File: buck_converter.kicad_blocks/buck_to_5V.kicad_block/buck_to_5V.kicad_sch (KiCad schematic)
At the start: 17 parts, among them U16 TPS54560BQDDARQ1

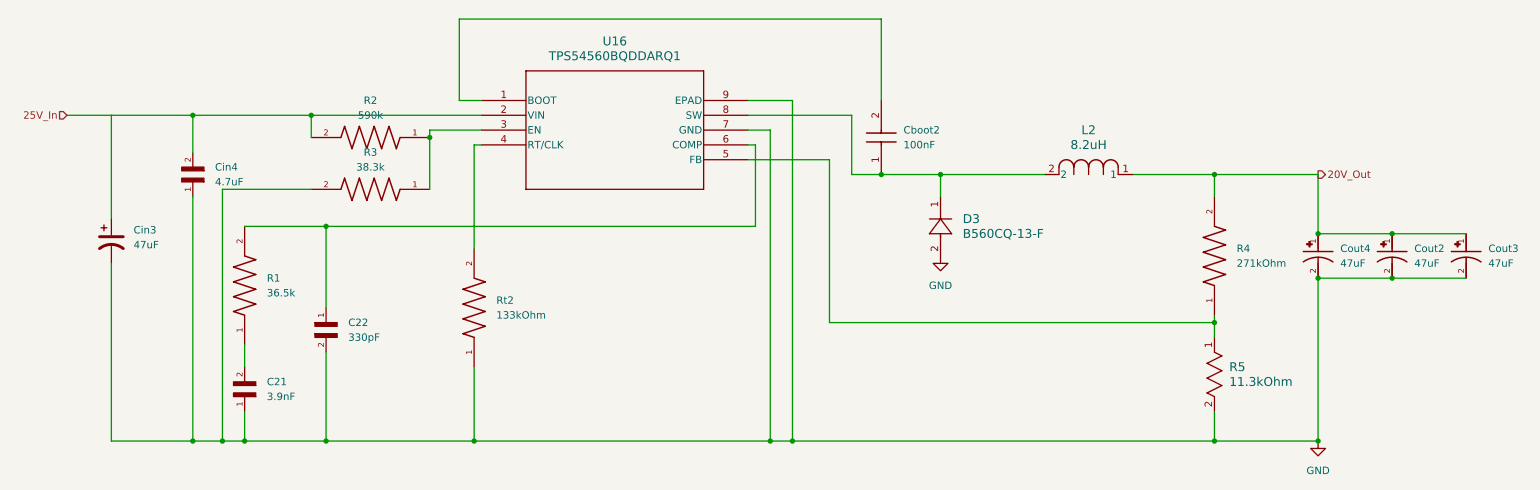
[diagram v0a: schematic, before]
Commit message: sry forgot to push, waiting on PCB shipping atm. Notes: split power distribution into two boards, one for the main 25V distribution, and another for 12V stuff. Also updated CAN transciever. the previous one was a 5V logic one (same logic as its power), and would have fried our ESPs data pins
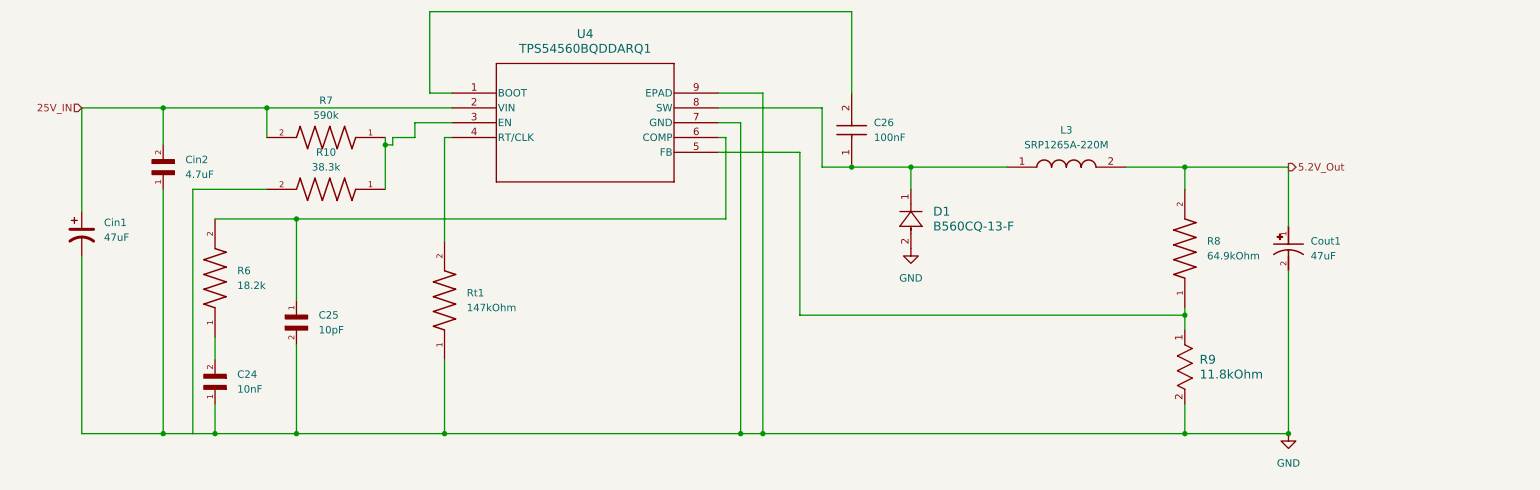
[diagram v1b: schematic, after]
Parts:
- removed C21: 3.9nF, Capacitor_SMD:C_0805_2012Metric_Pad1.18x1.45mm_HandSolder, symbol C0805C122J5GACTU:C0805C122J5GACTU
- removed C22: 330pF, Capacitor_SMD:C_0805_2012Metric_Pad1.18x1.45mm_HandSolder, symbol CL05C110JB5NNNC:CL05C110JB5NNNC
- removed Cboot2: 100nF, Capacitor_SMD:C_0805_2012Metric_Pad1.18x1.45mm_HandSolder, symbol 08053C104KAT2A:08053C104KAT2A
- removed Cin3: 47uF, Capacitor_SMD:CP_Elec_6.3x7.7, symbol Device:C_Polarized_US
- removed Cin4: 4.7uF, Capacitor_SMD:C_1210_3225Metric_Pad1.33x2.70mm_HandSolder, symbol GRM31CR71H475KA12L:GRM31CR71H475KA12L
- removed Cout2, Cout3, Cout4: 47uF, Capacitor_SMD:CP_Elec_6.3x7.7, symbol 10TPE47MAZB:10TPE47MAZB
- removed D3: B560CQ-13-F, Diode_SMD:D_SMC, symbol B560C-13-F:B560C-13-F
- removed L2: 8.2uH, Inductor_SMD:L_Vishay_IHLP-3232, symbol SRN8040-100M:SRN8040-100M
- removed R1: 36.5k, Resistor_SMD:R_0805_2012Metric_Pad1.20x1.40mm_HandSolder, symbol RC0201FR-0723K7L:RC0201FR-0723K7L
- removed R2: 590k, Resistor_SMD:R_0805_2012Metric_Pad1.20x1.40mm_HandSolder, symbol RC0201FR-0723K7L:RC0201FR-0723K7L
- removed R3: 38.3k, Resistor_SMD:R_0805_2012Metric_Pad1.20x1.40mm_HandSolder, symbol RC0201FR-0723K7L:RC0201FR-0723K7L
- removed R4: 271kOhm, Resistor_SMD:R_0805_2012Metric_Pad1.20x1.40mm_HandSolder, symbol CRCW040211K0FKED:CRCW040211K0FKED
- removed R5: 11.3kOhm, Resistor_SMD:R_0805_2012Metric_Pad1.20x1.40mm_HandSolder, symbol 2026-02-07_22-08-15:CRCW040261K9FKED
- removed Rt2: 133kOhm, Resistor_SMD:R_0805_2012Metric_Pad1.20x1.40mm_HandSolder, symbol CRCW0402118KFKED:CRCW0402118KFKED
- removed U16: TPS54560BQDDARQ1, Package_SO:SOIC-8-1EP_3.9x4.9mm_P1.27mm_EP2.29x3mm, symbol TPS54560BQDDARQ1:TPS54560BQDDARQ1
- added C24: 10nF, Capacitor_SMD:C_0805_2012Metric_Pad1.18x1.45mm_HandSolder, symbol C0805C122J5GACTU:C0805C122J5GACTU
- added C25: 10pF, Capacitor_SMD:C_0805_2012Metric_Pad1.18x1.45mm_HandSolder, symbol CL05C110JB5NNNC:CL05C110JB5NNNC
- added C26: 100nF, Capacitor_SMD:C_0805_2012Metric_Pad1.18x1.45mm_HandSolder, symbol 08053C104KAT2A:08053C104KAT2A
- added Cin1: 47uF, Capacitor_SMD:CP_Elec_6.3x7.7, symbol Device:C_Polarized_US
- added Cin2: 4.7uF, Capacitor_SMD:C_1210_3225Metric_Pad1.33x2.70mm_HandSolder, symbol GRM31CR71H475KA12L:GRM31CR71H475KA12L
- added Cout1: 47uF, Capacitor_Tantalum_SMD:CP_EIA-3528-21_Kemet-B_HandSolder, symbol 10TPE47MAZB:10TPE47MAZB
- added D1: B560CQ-13-F, Diode_SMD:D_SMC, symbol B560C-13-F:B560C-13-F
- added L3: SRP1265A-220M, PROVE-footprints:SRP1265A, symbol PROVE_Symbols:SRP1265A-220M
- added R10: 38.3k, Resistor_SMD:R_0805_2012Metric_Pad1.20x1.40mm_HandSolder, symbol RC0201FR-0723K7L:RC0201FR-0723K7L
- added R6: 18.2k, Resistor_SMD:R_0805_2012Metric_Pad1.20x1.40mm_HandSolder, symbol RC0201FR-0723K7L:RC0201FR-0723K7L
- added R7: 590k, Resistor_SMD:R_0805_2012Metric_Pad1.20x1.40mm_HandSolder, symbol RC0201FR-0723K7L:RC0201FR-0723K7L
- added R8: 64.9kOhm, Resistor_SMD:R_0805_2012Metric_Pad1.20x1.40mm_HandSolder, symbol CRCW040211K0FKED:CRCW040211K0FKED
- added R9: 11.8kOhm, Resistor_SMD:R_0805_2012Metric_Pad1.20x1.40mm_HandSolder, symbol 2026-02-07_22-08-15:CRCW040261K9FKED
- added Rt1: 147kOhm, Resistor_SMD:R_0805_2012Metric_Pad1.20x1.40mm_HandSolder, symbol CRCW0402118KFKED:CRCW0402118KFKED
- added U4: TPS54560BQDDARQ1, Package_SO:SOIC-8-1EP_3.9x4.9mm_P1.27mm_EP2.29x3mm, symbol TPS54560BQDDARQ1:TPS54560BQDDARQ1
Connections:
- net GND: now also C24.1, C25.2, Cin1.2, Cin2.1, Cout1.2, D1.2, R10.2, R9.2, Rt1.1, U4.7 (GND), U4.9 (EPAD)
- new net: C26.1, D1.1, L3.1, U4.8 (SW)
- new net: C26.2, U4.1 (BOOT)
- new net: R10.1, R7.1, U4.3 (EN)
- new net: Rt1.2, U4.4 (RT/CLK)
- new net: R8.1, R9.1, U4.5 (FB)
- new net: C25.1, R6.2, U4.6 (COMP)
- new net: C24.2, R6.1
- new net 25V_IN: Cin1.1, Cin2.2, R7.2, U4.2 (VIN)
- new net 5.2V_Out: Cout1.1, L3.2, R8.2

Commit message: updates to 12V, PDB, and IMU (leave me alone)
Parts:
- U4: Purchase Link https://www.mouser.com/en/ProductDetail/Texas-Instruments/T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 -> https://www.mouser.com/en/ProductDetail/Bourns/SRP1265A-220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
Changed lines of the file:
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@@
 			)
 		)
-		(property "Purchase Link" "https://www.mouser.com/en/ProductDetail/Texas-Instruments/TPS54560BQDDARQ1?qs=Mv7BduZupUi0AsDfghsxzg%3D%3D"
+		(property "Purchase Link" "https://www.mouser.com/en/ProductDetail/Bourns/SRP1265A-220M?qs=7z%252BmIopC6%2FIUC8RczBuOGQ%3D%3D"
 			(at 107.95 69.85 0)
 			(hide yes)
